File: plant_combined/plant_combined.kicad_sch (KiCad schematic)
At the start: 37 parts, among them J2 PJ-002AH, J3 Conn_01x02, U10 ZXBM5210-SP-13, U2 OLED_DISP, U8 PicoW, U9 AP62200WU-7

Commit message: Final tweak before release
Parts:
- removed R2, R3: 10K, Resistor_SMD:R_0805_2012Metric_Pad1.20x1.40mm_HandSolder, symbol Device:R
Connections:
- net +3.3V: no longer RV2.1
- net +3.3VA: now also RV2.1
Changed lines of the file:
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@@
   (junction (at 60.96 149.86) (diameter 0) (color 0 0 0 0)
   )
-  (junction (at 57.15 83.82) (diameter 0) (color 0 0 0 0)
-  )
   (junction (at 142.24 86.36) (diameter 0) (color 0 0 0 0)
   )
   (junction (at 77.47 128.27) (diameter 0) (color 0 0 0 0)
   )
-  (junction (at 76.2 88.9) (diameter 0) (color 0 0 0 0)
-  )
   (junction (at 212.09 140.97) (diameter 0) (color 0 0 0 0)
   )
@@
   (junction (at 269.24 119.38) (diameter 0) (color 0 0 0 0)
   )
-  (junction (at 72.39 91.44) (diameter 0) (color 0 0 0 0)
-  )
   (junction (at 85.09 144.78) (diameter 0) (color 0 0 0 0)
   )
@@
   )
   (junction (at 33.02 39.37) (diameter 0) (color 0 0 0 0)
-  )
-  (junction (at 154.94 53.34) (diameter 0) (color 0 0 0 0)
   )
   (junction (at 69.85 34.29) (diameter 0) (color 0 0 0 0)
@@
     (stroke (width 0) (type default))
   )
-  (wire (pts (xy 53.34 93.98) (xy 76.2 93.98))
-    (stroke (width 0) (type default))
-  )
   (wire (pts (xy 256.54 121.92) (xy 260.35 121.92))
     (stroke (width 0) (type default))
@@
     (stroke (width 0) (type default))
   )
-  (wire (pts (xy 53.34 91.44) (xy 53.34 93.98))
-    (stroke (width 0) (type default))
-  )
   (wire (pts (xy 41.91 128.27) (xy 54.61 128.27))
     (stroke (width 0) (type default))
@@
     (stroke (width 0) (type default))
   )
-  (wire (pts (xy 154.94 53.34) (xy 154.94 54.61))
+  (wire (pts (xy 154.94 50.8) (xy 154.94 54.61))
     (stroke (width 0) (type default))
   )
@@
     (stroke (width 0) (type default))
   )
-  (wire (pts (xy 60.96 91.44) (xy 72.39 91.44))
-    (stroke (width 0) (type default))
-  )
   (wire (pts (xy 60.96 135.89) (xy 63.5 135.89))
     (stroke (width 0) (type default))
@@
     (stroke (width 0) (type default))
   )
-  (wire (pts (xy 154.94 53.34) (xy 154.94 40.64))
-    (stroke (width 0) (type default))
-  )
   (wire (pts (xy 45.72 39.37) (xy 45.72 40.64))
     (stroke (width 0) (type default))
@@
     (stroke (width 0) (type default))
   )
-  (wire (pts (xy 76.2 93.98) (xy 76.2 88.9))
-    (stroke (width 0) (type default))
-  )
   (wire (pts (xy 30.48 31.75) (xy 62.23 31.75))
     (stroke (width 0) (type default))
@@
     (stroke (width 0) (type default))
   )
-  (wire (pts (xy 132.08 53.34) (xy 154.94 53.34))
-    (stroke (width 0) (type default))
-  )
   (polyline (pts (xy 182.88 158.75) (xy 16.51 158.75))
     (stroke (width 0) (type default))
@@
     (stroke (width 0) (type default))
   )
-  (wire (pts (xy 53.34 83.82) (xy 57.15 83.82))
-    (stroke (width 0) (type default))
-  )
   (wire (pts (xy 165.1 130.81) (xy 176.53 130.81))
     (stroke (width 0) (type default))
@@
     (stroke (width 0) (type default))
   )
-  (wire (pts (xy 57.15 83.82) (xy 57.15 82.55))
-    (stroke (width 0) (type default))
-  )
   (wire (pts (xy 96.52 148.59) (xy 96.52 144.78))
     (stroke (width 0) (type default))
   )
-  (wire (pts (xy 57.15 83.82) (xy 60.96 83.82))
+  (wire (pts (xy 147.32 52.07) (xy 147.32 53.34))
+    (stroke (width 0) (type default))
+  )
+  (wire (pts (xy 147.32 53.34) (xy 132.08 53.34))
     (stroke (width 0) (type default))
   )
@@
     )
   )
-  (symbol (lib_id "power:+3.3V") (at 57.15 82.55 0) (unit 1)
-    (in_bom yes) (on_board yes) (dnp no)
-    (property "Reference" "#PWR035" (at 57.15 86.36 0)
-      (effects (font (size 1.27 1.27)) hide)
-    )
-    (property "Value" "+3.3V" (at 55.88 78.74 0)
-      (effects (font (size 1.27 1.27)))
-    )
-    (property "Footprint" "" (at 57.15 82.55 0)
-      (effects (font (size 1.27 1.27)) hide)
-    )
-    (property "Datasheet" "" (at 57.15 82.55 0)
-      (effects (font (size 1.27 1.27)) hide)
-    )
-    (pin "1")
-    (instances
-      (project "plant_combined"
-        (path "/0c0a9329-c070-44ba-a98c-07a53ea4a4f2"
-          (reference "#PWR035") (unit 1)
-        )
-      )
-      (project "plant_waterer"
-        (path "/c45c0694-9602-4b56-aa7f-43745d5d08c4"
-          (reference "#PWR018") (unit 1)
-        )
-      )
-    )
-  )
   (symbol (lib_id "power:GND") (at 129.54 151.13 0) (unit 1)
     (in_bom yes) (on_board yes) (dnp no) (fields_autoplaced)
@@
         (path "/efe00140-c2a9-43c9-8a91-2dc458d0d3a7"
           (reference "#PWR012") (unit 1)
-        )
-      )
-    )
-  )
-  (symbol (lib_id "power:+3.3V") (at 154.94 40.64 0) (unit 1)
-    (in_bom yes) (on_board yes) (dnp no)
-    (property "Reference" "#PWR042" (at 154.94 44.45 0)
-      (effects (font (size 1.27 1.27)) hide)
-    )
-    (property "Value" "+3.3V" (at 153.67 36.83 0)
-      (effects (font (size 1.27 1.27)))
-    )
-    (property "Footprint" "" (at 154.94 40.64 0)
-      (effects (font (size 1.27 1.27)) hide)
-    )
-    (property "Datasheet" "" (at 154.94 40.64 0)
-      (effects (font (size 1.27 1.27)) hide)
-    )
-    (pin "1")
-    (instances
-      (project "plant_combined"
-        (path "/0c0a9329-c070-44ba-a98c-07a53ea4a4f2"
-          (reference "#PWR042") (unit 1)
-        )
-      )
-      (project "plant_waterer"
-        (path "/c45c0694-9602-4b56-aa7f-43745d5d08c4"
-          (reference "#PWR05") (unit 1)
         )
       )
@@
     )
   )
+  (symbol (lib_id "power:+3.3VA") (at 154.94 50.8 0) (unit 1)
+    (in_bom yes) (on_board yes) (dnp no) (fields_autoplaced)
+    (property "Reference" "#PWR033" (at 154.94 54.61 0)
+      (effects (font (size 1.27 1.27)) hide)
+    )
+    (property "Value" "+3.3VA" (at 154.94 46.99 0)
+      (effects (font (size 1.27 1.27)))
+    )
+    (property "Footprint" "" (at 154.94 50.8 0)
+      (effects (font (size 1.27 1.27)) hide)
+    )
+    (property "Datasheet" "" (at 154.94 50.8 0)
+      (effects (font (size 1.27 1.27)) hide)
+    )
+    (pin "1")
+    (instances
+      (project "plant_combined"
+        (path "/0c0a9329-c070-44ba-a98c-07a53ea4a4f2/bd86b945-c087-489f-87da-de931ba4c915"
+          (reference "#PWR033") (unit 1)
+        )
+        (path "/0c0a9329-c070-44ba-a98c-07a53ea4a4f2"
+          (reference "#PWR036") (unit 1)
+        )
+      )
+    )
+  )
   (symbol (lib_id "power:GND") (at 101.6 144.78 0) (unit 1)
     (in_bom yes) (on_board yes) (dnp no) (fields_autoplaced)
@@
     )
   )
-  (symbol (lib_id "Device:R") (at 60.96 87.63 0) (unit 1)
-    (in_bom yes) (on_board yes) (dnp no) (fields_autoplaced)
-    (property "Reference" "R2" (at 63.5 86.3599 0)
-      (effects (font (size 1.27 1.27)) (justify left))
-    )
-    (property "Value" "10K" (at 63.5 88.8999 0)
-      (effects (font (size 1.27 1.27)) (justify left))
-    )
-    (property "Footprint" "Resistor_SMD:R_0805_2012Metric_Pad1.20x1.40mm_HandSolder" (at 59.182 87.63 90)
-      (effects (font (size 1.27 1.27)) hide)
-    )
-    (property "Datasheet" "~" (at 60.96 87.63 0)
-      (effects (font (size 1.27 1.27)) hide)
-    )
-    (pin "1")
-    (pin "2")
-    (instances
-      (project "plant_combined"
-        (path "/0c0a9329-c070-44ba-a98c-07a53ea4a4f2"
-          (reference "R2") (unit 1)
-        )
-      )
-      (project "plant_waterer"
-        (path "/c45c0694-9602-4b56-aa7f-43745d5d08c4"
-          (reference "R3") (unit 1)
-        )
-      )
-    )
-  )
   (symbol (lib_id "power:GND") (at 85.09 93.98 0) (unit 1)
     (in_bom yes) (on_board yes) (dnp no) (fields_autoplaced)
@@
         (path "/c45c0694-9602-4b56-aa7f-43745d5d08c4"
           (reference "#PWR013") (unit 1)
-        )
-      )
-    )
-  )
-  (symbol (lib_id "Device:R") (at 53.34 87.63 0) (unit 1)
-    (in_bom yes) (on_board yes) (dnp no)
-    (property "Reference" "R3" (at 55.88 86.3599 0)
-      (effects (font (size 1.27 1.27)) (justify left))
-    )
-    (property "Value" "10K" (at 55.88 88.8999 0)
-      (effects (font (size 1.27 1.27)) (justify left))
-    )
-    (property "Footprint" "Resistor_SMD:R_0805_2012Metric_Pad1.20x1.40mm_HandSolder" (at 51.562 87.63 90)
-      (effects (font (size 1.27 1.27)) hide)
-    )
-    (property "Datasheet" "~" (at 53.34 87.63 0)
-      (effects (font (size 1.27 1.27)) hide)
-    )
-    (pin "1")
-    (pin "2")
-    (instances
-      (project "plant_combined"
-        (path "/0c0a9329-c070-44ba-a98c-07a53ea4a4f2"
-          (reference "R3") (unit 1)
-        )
-      )
-      (project "plant_waterer"
-        (path "/c45c0694-9602-4b56-aa7f-43745d5d08c4"
-          (reference "R2") (unit 1)
         )
       )
@@
         )
       )
+    )
+  )
+  (symbol (lib_id "power:+3.3V") (at 147.32 52.07 0) (unit 1)
+    (in_bom yes) (on_board yes) (dnp no)
+    (property "Reference" "#PWR042" (at 147.32 55.88 0)
+      (effects (font (size 1.27 1.27)) hide)
+    )
+    (property "Value" "+3.3V" (at 146.05 48.26 0)
+      (effects (font (size 1.27 1.27)))
+    )
+    (property "Footprint" "" (at 147.32 52.07 0)
+      (effects (font (size 1.27 1.27)) hide)
+    )
+    (property "Datasheet" "" (at 147.32 52.07 0)
+      (effects (font (size 1.27 1.27)) hide)
+    )
+    (pin "1")
+    (instances
+      (project "plant_combined"
+        (path "/0c0a9329-c070-44ba-a98c-07a53ea4a4f2"
+          (reference "#PWR042") (unit 1)
+        )
+      )
+      (project "plant_waterer"
+        (path "/c45c0694-9602-4b56-aa7f-43745d5d08c4"
+          (reference "#PWR05") (unit 1)
+        )
+      )

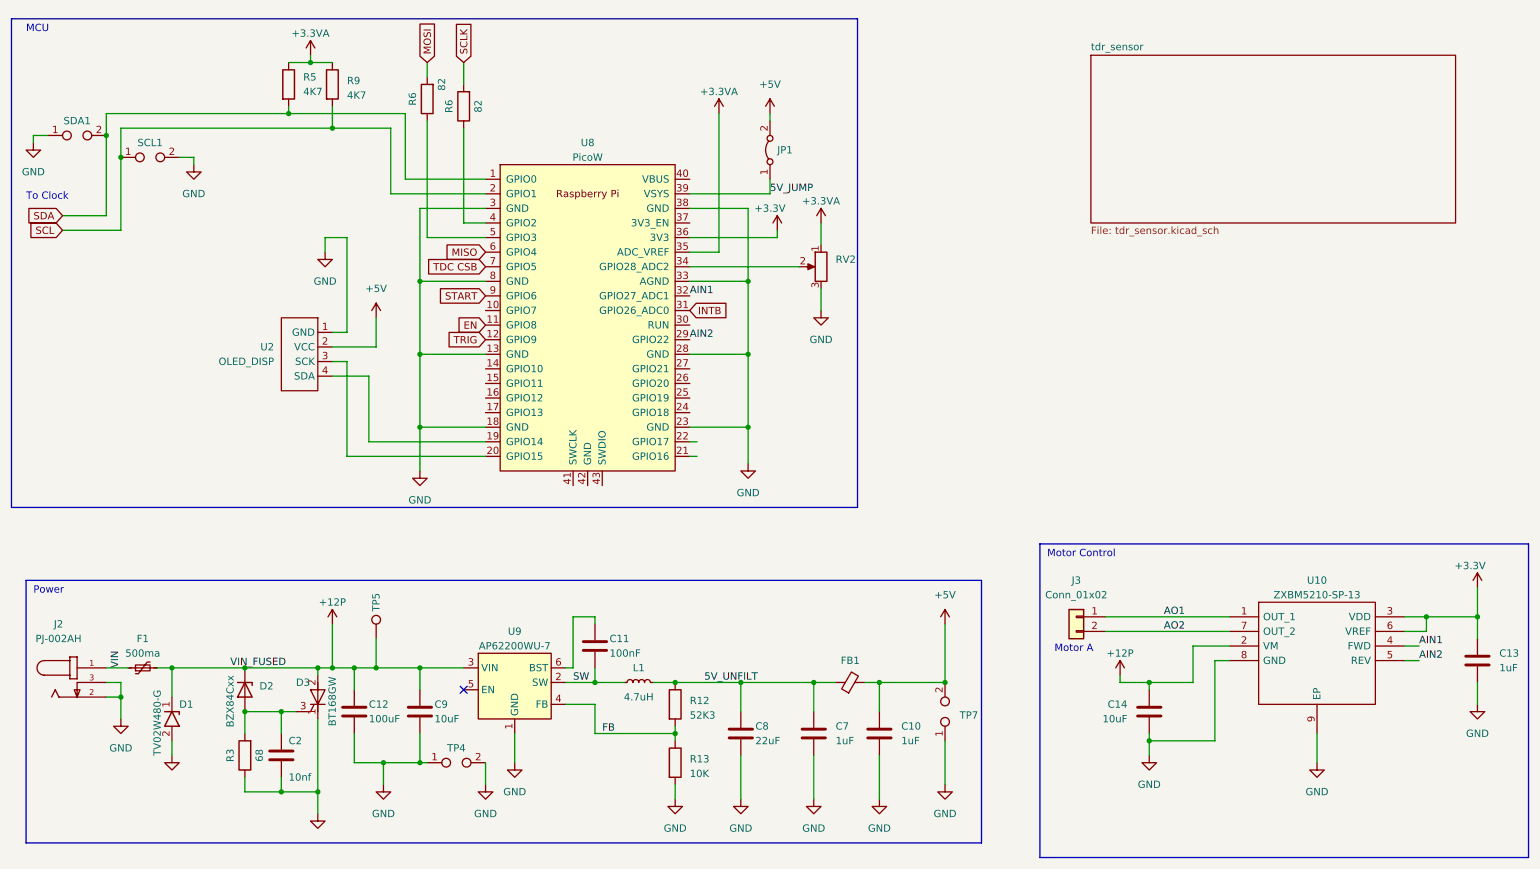
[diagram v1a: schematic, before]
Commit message: Add pull-up to MISO
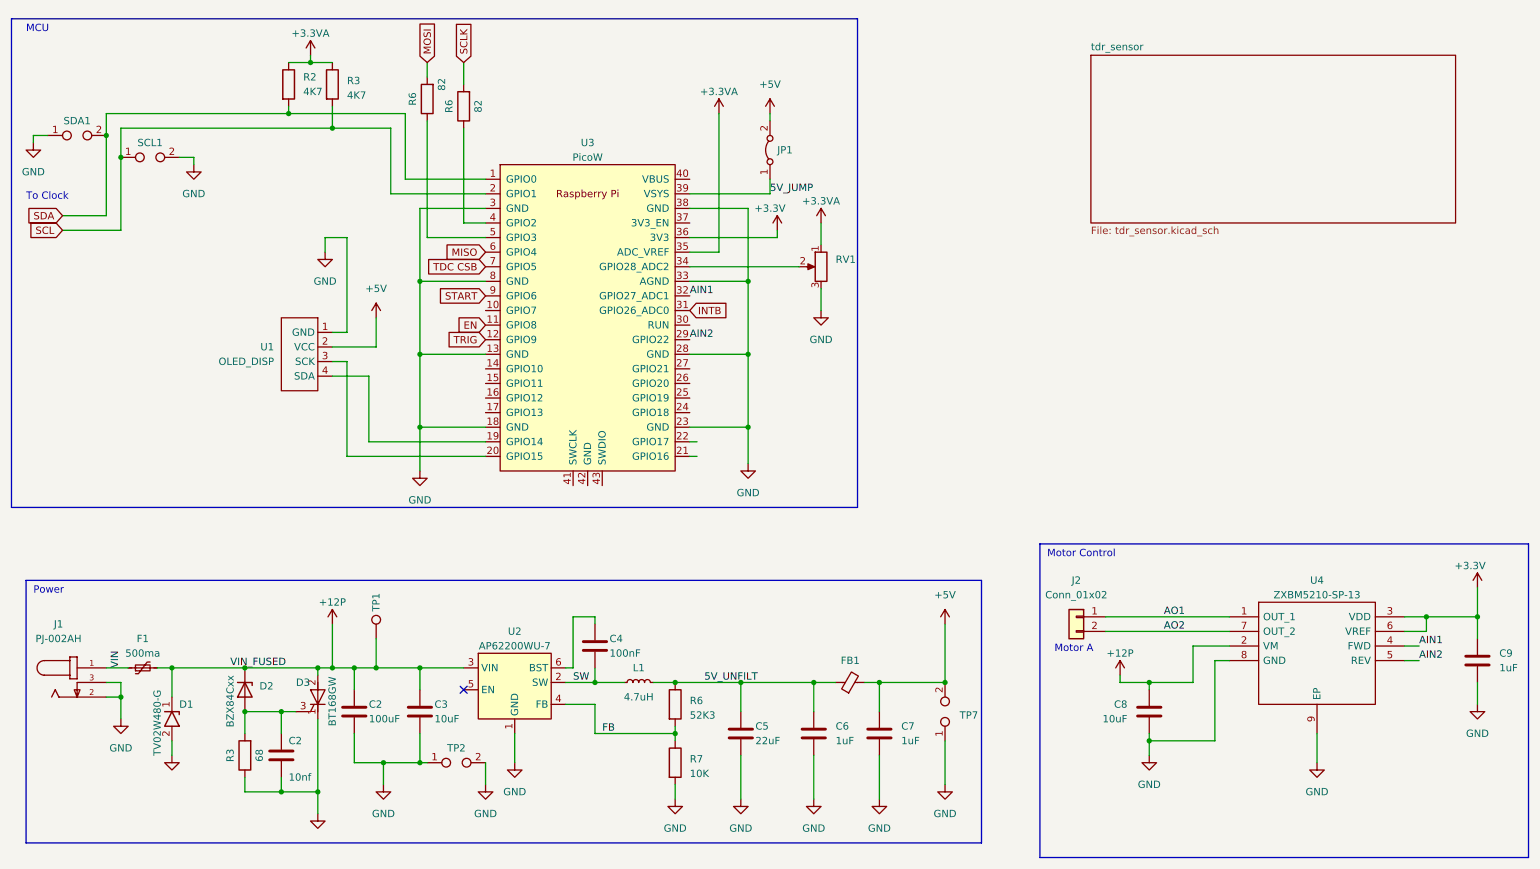
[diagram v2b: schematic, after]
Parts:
- renumbered C12 to C2, C9 to C3, C11 to C4, C8 to C5, C7 to C6, C10 to C7, C14 to C8, C13 to C9, J2 to J1, J3 to J2, R5 to R2, R9 to R3, R12 to R6, R13 to R7, RV2 to RV1, TP5 to TP1, TP4 to TP2, U2 to U1, U9 to U2, U8 to U3, U10 to U4
